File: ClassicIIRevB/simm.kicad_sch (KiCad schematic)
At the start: 4 parts, among them J12 DRAM SIMM

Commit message: Switch to some "official" net names
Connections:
- net BD16 renamed RD0
- net BD17 renamed RD1
- net BD18 renamed RD2
- net BD19 renamed RD3
- net BD20 renamed RD4
- net BD21 renamed RD5
- net BD22 renamed RD6
- net BD23 renamed RD7
- net BD24 renamed RD8
- net BD25 renamed RD9
- net BD26 renamed RD10
- net BD27 renamed RD11
- net BD28 renamed RD12
- net BD29 renamed RD13
- net BD30 renamed RD14
- net BD31 renamed RD15
- net ~{CAS1H} renamed ~{CAS0H}
- net ~{CAS1L} renamed ~{CAS0L}
- net ~{RAS1} renamed ~{RAS0}
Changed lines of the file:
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@@
+		)
+	)
+	(label "RD3"
+		(at 104.14 92.71 0)
+		(effects
+			(font
+				(size 1.27 1.27)
+			)
+			(justify left bottom)
+		)
+	)
+	(label "RD14"
+		(at 172.72 119.38 180)
+		(effects
+			(font
+				(size 1.27 1.27)
+			)
+			(justify right bottom)
 		)
 	)
@@
 		)
 	)
-	(label "BD16"
-		(at 104.14 67.31 0)
-		(effects
-			(font
-				(size 1.27 1.27)
-			)
-			(justify left bottom)
-		)
-	)
-	(label "BD17"
-		(at 104.14 74.93 0)
+	(label "RD7"
+		(at 104.14 124.46 0)
 		(effects
 			(font
@@
 		)
 	)
-	(label "BD28"
-		(at 172.72 100.33 180)
-		(effects
-			(font
-				(size 1.27 1.27)
-			)
-			(justify right bottom)
-		)
-	)
-	(label "BD31"
-		(at 172.72 124.46 180)
-		(effects
-			(font
-				(size 1.27 1.27)
-			)
-			(justify right bottom)
-		)
-	)
-	(label "BD21"
-		(at 104.14 111.76 0)
-		(effects
-			(font
-				(size 1.27 1.27)
-			)
-			(justify left bottom)
-		)
-	)
-	(label "BD30"
-		(at 172.72 119.38 180)
-		(effects
-			(font
-				(size 1.27 1.27)
-			)
-			(justify right bottom)
-		)
-	)
-	(label "BD19"
-		(at 104.14 92.71 0)
-		(effects
-			(font
-				(size 1.27 1.27)
-			)
-			(justify left bottom)
-		)
-	)
 	(label "BRA1"
 		(at 160.02 73.66 180)
@@
 		)
 	)
-	(label "BD25"
-		(at 172.72 74.93 180)
+	(label "RD11"
+		(at 172.72 92.71 180)
 		(effects
 			(font
@@
 		)
 	)
-	(label "BD27"
-		(at 172.72 92.71 180)
-		(effects
-			(font
-				(size 1.27 1.27)
-			)
-			(justify right bottom)
-		)
-	)
 	(label "BRA5"
 		(at 160.02 91.44 180)
@@
 		)
 	)
-	(label "BD22"
-		(at 104.14 119.38 0)
+	(label "RD0"
+		(at 104.14 67.31 0)
+		(effects
+			(font
+				(size 1.27 1.27)
+			)
+			(justify left bottom)
+		)
+	)
+	(label "RD1"
+		(at 104.14 74.93 0)
 		(effects
 			(font
@@
 		)
 	)
-	(label "BD20"
-		(at 104.14 100.33 0)
-		(effects
-			(font
-				(size 1.27 1.27)
-			)
-			(justify left bottom)
-		)
-	)
 	(label "BRA10"
 		(at 160.02 109.22 180)
@@
 		)
 	)
+	(label "RD2"
+		(at 104.14 85.09 0)
+		(effects
+			(font
+				(size 1.27 1.27)
+			)
+			(justify left bottom)
+		)
+	)
 	(label "BRA1"
 		(at 116.84 73.66 0)
@@
 		)
 	)
-	(label "BD18"
-		(at 104.14 85.09 0)
-		(effects
-			(font
-				(size 1.27 1.27)
-			)
-			(justify left bottom)
-		)
-	)
-	(label "BD26"
-		(at 172.72 85.09 180)
-		(effects
-			(font
-				(size 1.27 1.27)
-			)
-			(justify right bottom)
-		)
-	)
 	(label "BRA3"
 		(at 160.02 81.28 180)
@@
 		)
 	)
+	(label "RD6"
+		(at 104.14 119.38 0)
+		(effects
+			(font
+				(size 1.27 1.27)
+			)
+			(justify left bottom)
+		)
+	)
 	(label "BRA2"
 		(at 160.02 78.74 180)
@@
 		)
 	)
-	(label "BD23"
-		(at 104.14 124.46 0)
-		(effects
-			(font
-				(size 1.27 1.27)
-			)
-			(justify left bottom)
+	(label "RD4"
+		(at 104.14 100.33 0)
+		(effects
+			(font
+				(size 1.27 1.27)
+			)
+			(justify left bottom)
+		)
+	)
+	(label "RD8"
+		(at 172.72 67.31 180)
+		(effects
+			(font
+				(size 1.27 1.27)
+			)
+			(justify right bottom)
+		)
+	)
+	(label "RD13"
+		(at 172.72 111.76 180)
+		(effects
+			(font
+				(size 1.27 1.27)
+			)
+			(justify right bottom)
 		)
 	)
@@
 		)
 	)
-	(label "BD24"
-		(at 172.72 67.31 180)
-		(effects
-			(font
-				(size 1.27 1.27)
-			)
-			(justify right bottom)
-		)
-	)
-	(label "BD29"
-		(at 172.72 111.76 180)
+	(label "RD15"
+		(at 172.72 124.46 180)
+		(effects
+			(font
+				(size 1.27 1.27)
+			)
+			(justify right bottom)
+		)
+	)
+	(label "RD10"
+		(at 172.72 85.09 180)
 		(effects
 			(font
@@
 		)
 	)
-	(global_label "~{CAS1H}"
+	(label "RD9"
+		(at 172.72 74.93 180)
+		(effects
+			(font
+				(size 1.27 1.27)
+			)
+			(justify right bottom)
+		)
+	)
+	(label "RD12"
+		(at 172.72 100.33 180)
+		(effects
+			(font
+				(size 1.27 1.27)
+			)
+			(justify right bottom)
+		)
+	)
+	(label "RD5"
+		(at 104.14 111.76 0)
+		(effects
+			(font
+				(size 1.27 1.27)
+			)
+			(justify left bottom)
+		)
+	)
+	(global_label "~{CAS0H}"
 		(shape input)
 		(at 38.1 55.88 180)
@@
 		)
 	)
-	(global_label "~{CAS1L}"
+	(global_label "~{CAS0L}"
 		(shape input)
 		(at 38.1 60.96 180)
@@
 		)
 	)
-	(global_label "~{RAS1}"
+	(global_label "~{RAS0}"
 		(shape input)
 		(at 38.1 139.7 180)
@@
 		)
 	)
-	(global_label "BD[16..31]"
+	(global_label "RD[0..15]"
 		(shape output)
 		(at 241.3 149.86 0)
@@
 		)
 	)
-	(global_label "BD[16..31]"
+	(global_label "RD[0..15]"
 		(shape input)
 		(at 38.1 149.86 180)

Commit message: update exports
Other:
- title: Macintosh Classic II Revision B -> Macintosh Classic II (Later Revision)
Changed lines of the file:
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@@
 	(paper "USLetter")
 	(title_block
-		(title "Macintosh Classic II Revision B")
-		(date "2025-06-04")
+		(title "Macintosh Classic II (Later Revision)")
+		(date "2025-06-16")
 		(company "Apple Computer")
 		(comment 1 "drawn by Bradley Bell")

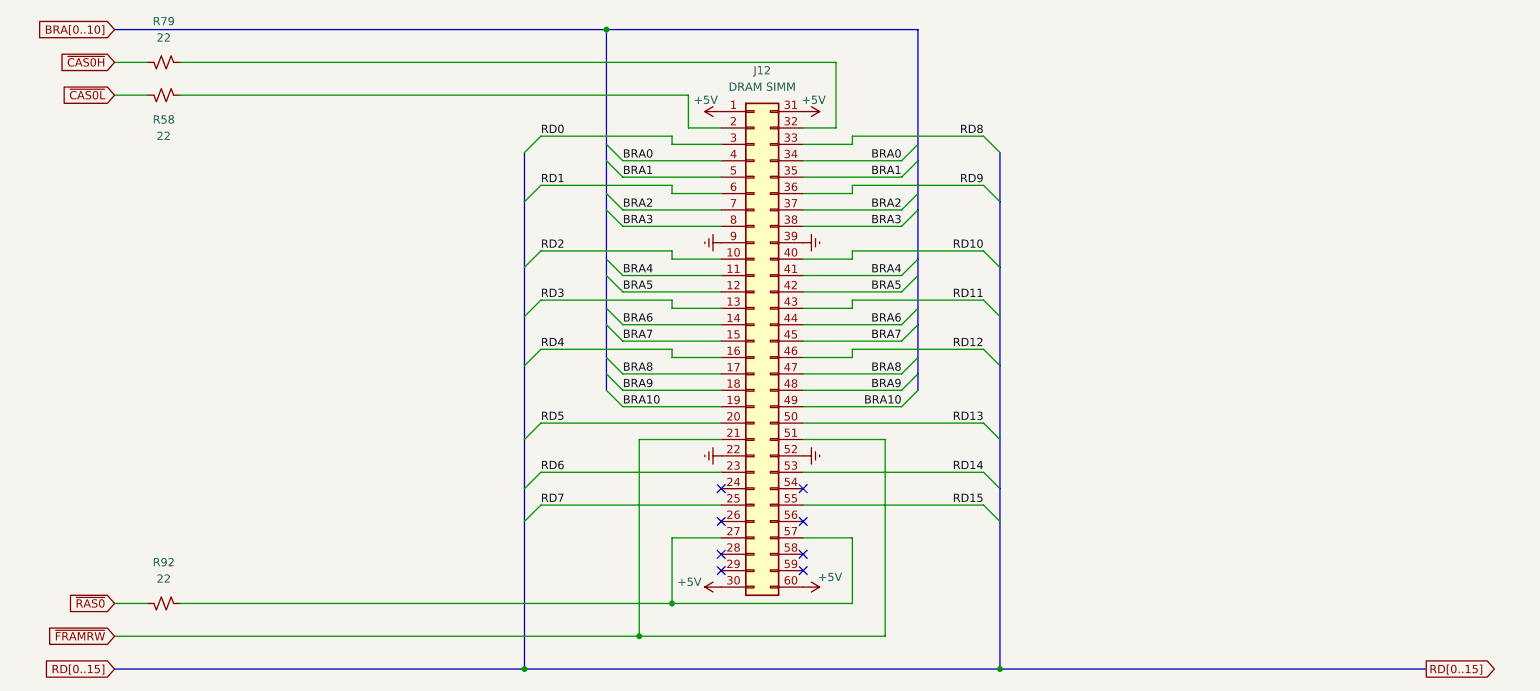
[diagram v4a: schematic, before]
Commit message: Corrections to SMDs, more improved footprints
The later revision board reproduction design is now complete.
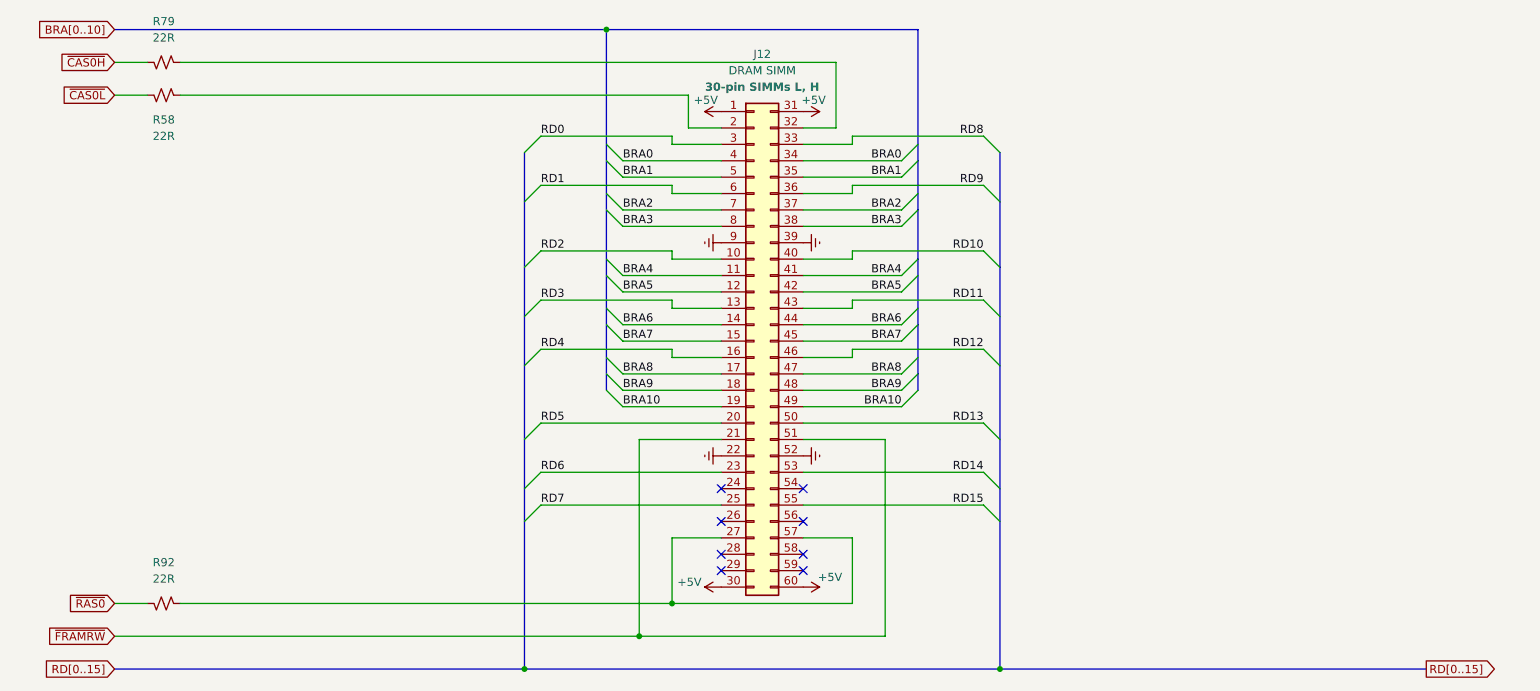
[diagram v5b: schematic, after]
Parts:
- R58, R79, R92: value 22 -> 22R
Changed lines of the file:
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@@
 	(title_block
 		(title "Macintosh Classic II (Later Revision)")
-		(date "2025-06-16")
+		(date "2025-06-21")
 		(company "Apple Computer")
 		(comment 1 "drawn by Bradley Bell")
@@
 		)
 		(property "Intersheetrefs" "${INTERSHEET_REFS}"
-			(at 254.5662 149.86 0)
+			(at 253.3567 149.86 0)
 			(effects
 				(font
@@
 		)
 		(property "Intersheetrefs" "${INTERSHEET_REFS}"
-			(at 24.8338 149.86 0)
+			(at 26.0433 149.86 0)
 			(effects
 				(font
@@
 			)
 		)
-		(property "Value" "22"
+		(property "Value" "22R"
 			(at 45.72 67.31 90)
 			(effects
@@
 		(fields_autoplaced yes)
 		(property "Reference" "J12"
+			(at 138.43 54.61 0)
+			(effects
+				(font
+					(size 1.27 1.27)
+				)
+			)
+		)
+		(property "Value" "DRAM SIMM"
 			(at 138.43 57.15 0)
-			(effects
-				(font
-					(size 1.27 1.27)
-				)
-			)
-		)
-		(property "Value" "DRAM SIMM"
-			(at 138.43 59.69 0)
 			(effects
 				(font
@@
 			)
 		)
-		(property "Description" "Generic connector, double row, 02x30, top/bottom pin numbering scheme (row 1: 1...pins_per_row, row2: pins_per_row+1 ... num_pins), script generated (kicad-library-utils/schlib/autogen/connector/)"
-			(at 137.16 99.06 0)
-			(effects
-				(font
-					(size 1.27 1.27)
-				)
-				(hide yes)
+		(property "Description" "30-pin SIMMs L, H"
+			(at 138.43 59.69 0)
+			(effects
+				(font
+					(size 1.27 1.27)
+					(thickness 0.254)
+					(bold yes)
+				)
 			)
 		)
@@
 			)
 		)
-		(property "Value" "22"
+		(property "Value" "22R"
 			(at 45.72 52.07 90)
 			(effects
@@
 			)
 		)
-		(property "Value" "22"
+		(property "Value" "22R"
 			(at 45.72 135.89 90)
 			(effects
